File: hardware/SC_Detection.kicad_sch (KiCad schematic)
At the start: 46 parts, among them U11 REF2033, U12 LMV393LV, U13 INA181, U15 LMV393LV, U16 INA181, U17 LMV393LV, U18 INA181, U22 LMV393LV, U25 INA181

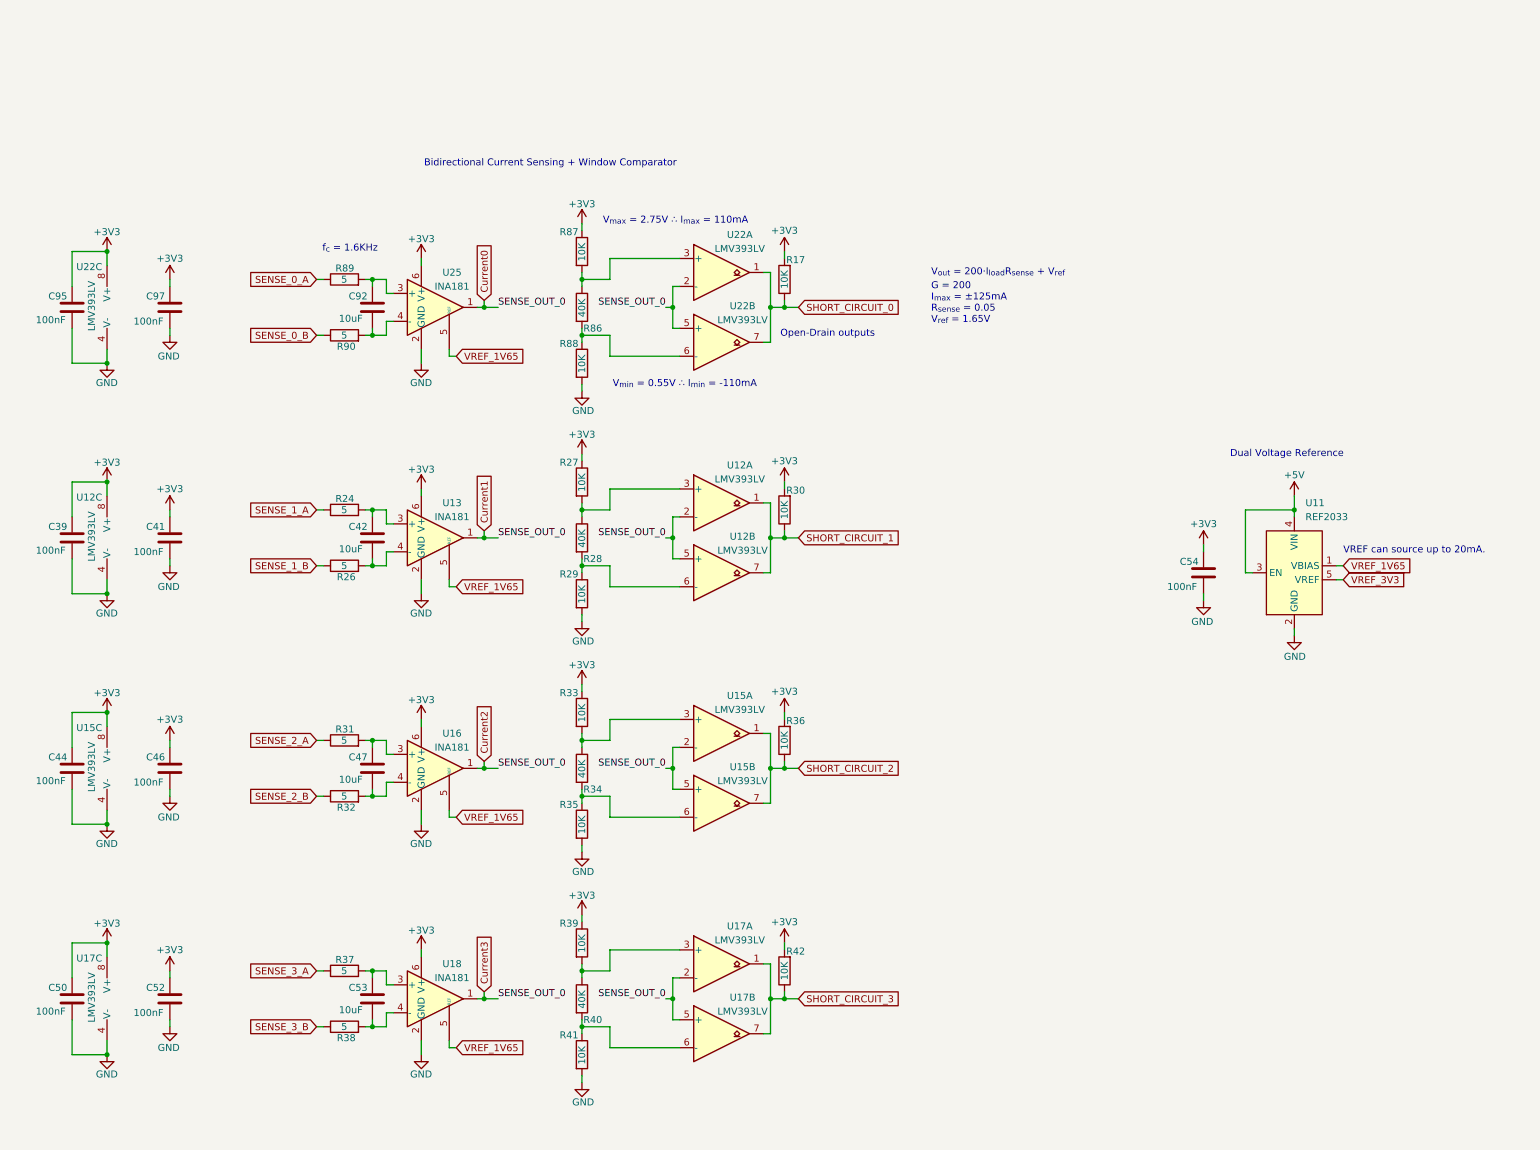
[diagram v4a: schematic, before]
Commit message: update short detection; draft bom
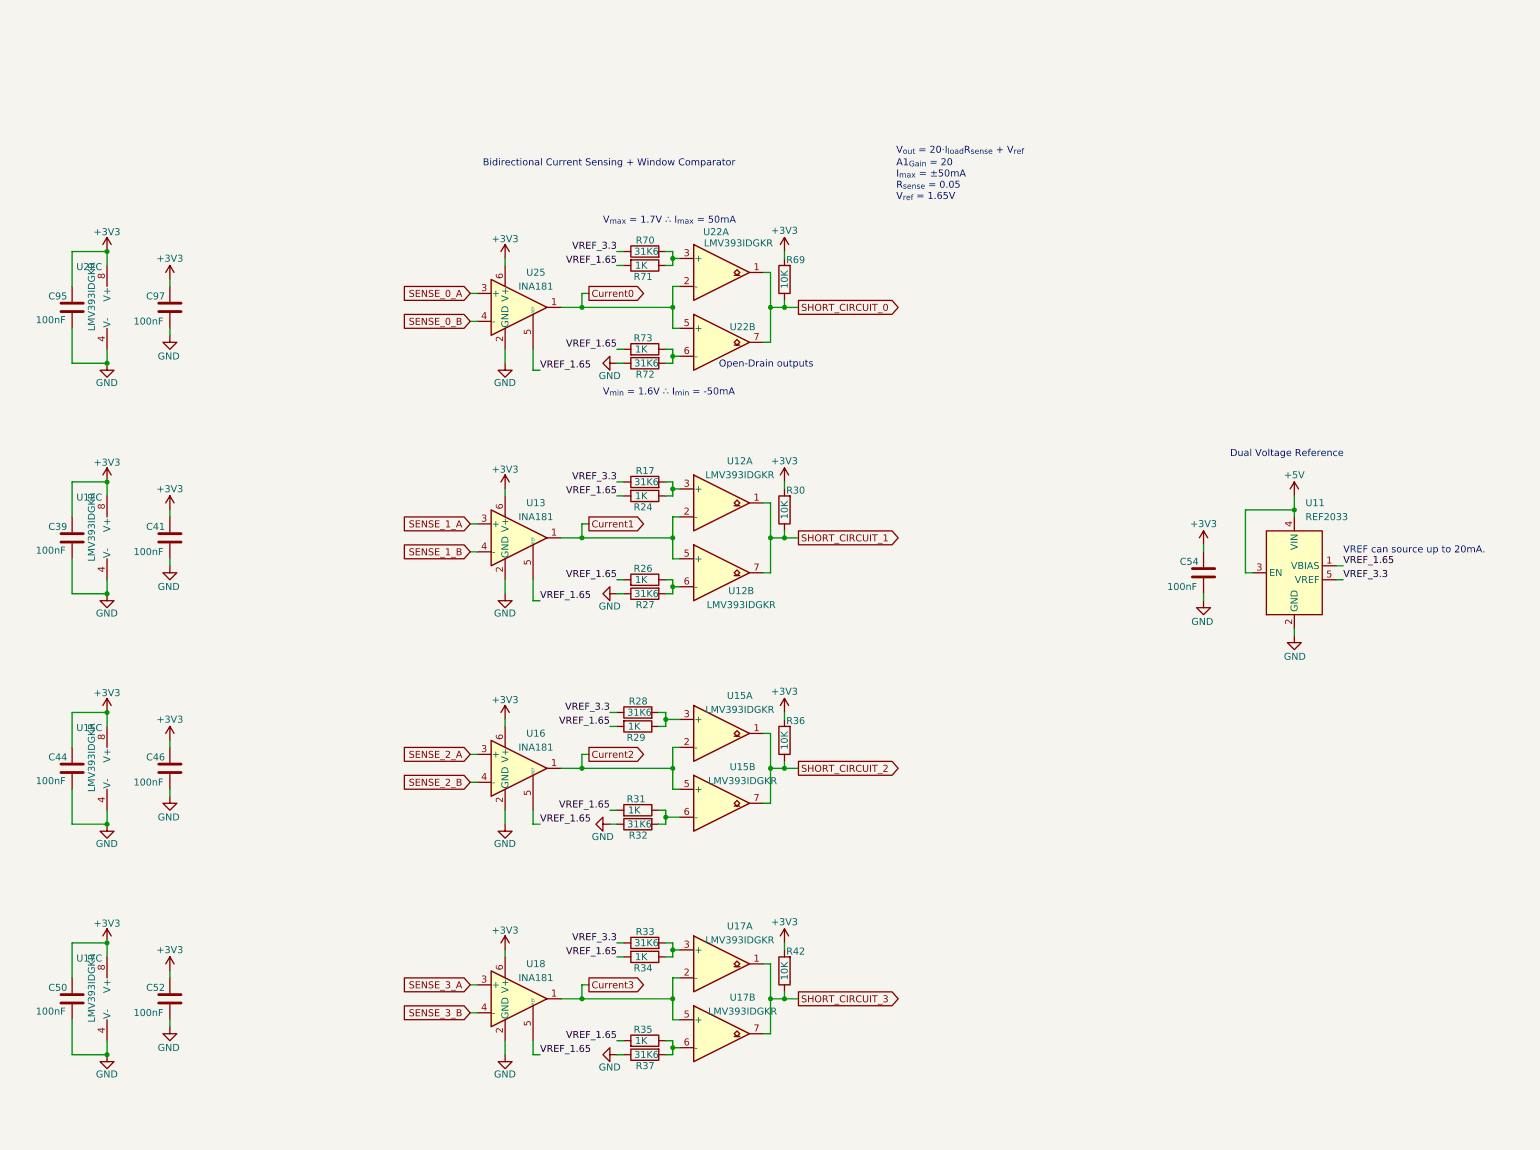
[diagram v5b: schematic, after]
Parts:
- removed C42, C47, C53, C92: 10uF, symbol Device:C
- removed R38, R89, R90: 5, symbol Device:R
- removed R39, R41, R87, R88: 10K, symbol Device:R
- removed R40, R86: 40K, symbol Device:R
- added R69: 10K, Resistor_SMD:R_0402_1005Metric, symbol Device:R
- added R70, R72: 31K6, Resistor_SMD:R_0402_1005Metric, symbol Device:R
- added R71, R73: 1K, Resistor_SMD:R_0402_1005Metric, symbol Device:R
- C39, C41, C44, C46, C50, C52, C54, C95, C97: footprint (none) -> Capacitor_SMD:C_0402_1005Metric; Link (none) -> https://www.digikey.com/en/products/detail/murata-electroni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; Manufacturer (none) -> Murata Electronics; Manufacturer Number (none) -> GRM155R71H104KE14D; Temperature Coefficient (none) -> X7R
- R17, R27, R33: value 10K -> 31K6; footprint (none) -> Resistor_SMD:R_0402_1005Metric
- R24, R26, R31: value 5 -> 1K; footprint (none) -> Resistor_SMD:R_0402_1005Metric
- R28: value 40K -> 31K6; footprint (none) -> Resistor_SMD:R_0402_1005Metric
- R29, R35: value 10K -> 1K; footprint (none) -> Resistor_SMD:R_0402_1005Metric
- R30, R36, R42: footprint (none) -> Resistor_SMD:R_0402_1005Metric
- R32, R37: value 5 -> 31K6; footprint (none) -> Resistor_SMD:R_0402_1005Metric
- R34: value 40K -> 1K; footprint (none) -> Resistor_SMD:R_0402_1005Metric
- U12, U15, U17, U22: value LMV393LV -> LMV393IDGKR; footprint (none) -> Package_SO:VSSOP-8_3x3mm_P0.65mm; Link (none) -> https://www.ti.com/general/docs/suppproductinfo.tsp?distId=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; Manufacturer Number LM393LVPWR -> LMV393IDGKR
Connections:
- net VREF_1V65 is gone; now on net VREF_1.65: U11.1 (VBIAS), U13.5 (REF), U16.5 (REF), U18.5 (REF), U25.5 (REF)
- net +3V3: now also R69.2; no longer R17.2, R27.1, R33.1
- net Current0: no longer U12.2 (-), U12.5 (+), U13.1, U15.2 (-), U15.5 (+), U16.1, U17.2 (-), U17.5 (+), U18.1
- net GND: now also R27.1, R32.1, R37.1, R72.1; no longer R29.2, R35.2
- net SENSE_0_A: now also U25.3 (+)
- net SENSE_0_B: now also U25.4 (-)
- net SENSE_1_A: now also U13.3 (+); no longer R24.1
- net SENSE_1_B: now also U13.4 (-); no longer R26.1
- net SENSE_2_A: now also U16.3 (+); no longer R31.1
- net SENSE_2_B: now also U16.4 (-); no longer R32.1
- net SENSE_3_A: now also U18.3 (+); no longer R37.1
- net SENSE_3_B: now also U18.4 (-)
- net SHORT_CIRCUIT_0: now also R69.1; no longer R17.1
- net at U22.3 (+): now also R70.2, R71.1
- net at U22.6 (-): now also R72.2, R73.1
- net at R28.2, R29.1: now also U15.3 (+); no longer U12.6 (-)
- net at R37.2: now also R35.1, U17.6 (-); no longer U18.3 (+)
- net at R33.2, R34.1: now also U17.3 (+); no longer U15.3 (+)
- net VREF_1.65: now reaches R24.2
- net VREF_1.65: now also R26.2, R29.2, R31.2, R34.2, R35.2, R71.2, R73.2; no longer U13.3 (+)
- net at R32.2: now also R31.1, U15.6 (-); no longer U16.4 (-)
- net VREF_3V3 renamed VREF_3.3
- net VREF_3.3: now also R17.1, R28.1, R33.1, R70.1
- new net: R26.1, R27.2, U12.6 (-)
- new net: R17.2, R24.1, U12.3 (+)
- new net Current1: U12.2 (-), U12.5 (+), U13.1
- new net Current2: U15.2 (-), U15.5 (+), U16.1
- new net Current3: U17.2 (-), U17.5 (+), U18.1
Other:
- note added: "A1_{Gain} = 20 I_{max} = ±50mA R_{sense} = 0.05 V_{ref} = 1.65V"
- note added: "V_{max} = 1.7V ∴ I_{max} = 50mA"
- note added: "V_{min} = 1.6V ∴ I_{min} = -50mA"
- note added: "V_{out} = 20·I_{load}R_{sense} + V_{ref}"
- note removed: "G = 200 I_{max} = ±125mA R_{sense} = 0.05 V_{ref} = 1.65V"
- note removed: "V_{max} = 2.75V ∴ I_{max} = 110mA"
- note removed: "V_{min} = 0.55V ∴ I_{min} = -110mA"
- note removed: "V_{out} = 200·I_{load}R_{sense} + V_{ref}"
- note removed: "f_{c} = 1.6KHz"
- moved on the sheet: U13, U16, U18, U25

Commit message: update board draft
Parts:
- renumbered C95 to C50, C39 to C51, C44 to C52, C50 to C53, C97 to C54, C41 to C55, C46 to C56, C52 to C57, C54 to C58, R28 to R39, R29 to R40, R31 to R41, R32 to R42, R70 to R43, R71 to R44, R73 to R45, R72 to R46, R17 to R47, R24 to R48, R26 to R49, R27 to R50, R33 to R51, R34 to R52, R35 to R53, R37 to R54, R69 to R55, R30 to R56, R36 to R57, R42 to R58, U22 to U13, U12 to U14, U17 to U16, U25 to U17, U13 to U18, U16 to U19, U18 to U20, U11 to U21
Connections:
- net +3V3 renamed +3.3V
- net +3.3V: no longer R58.2

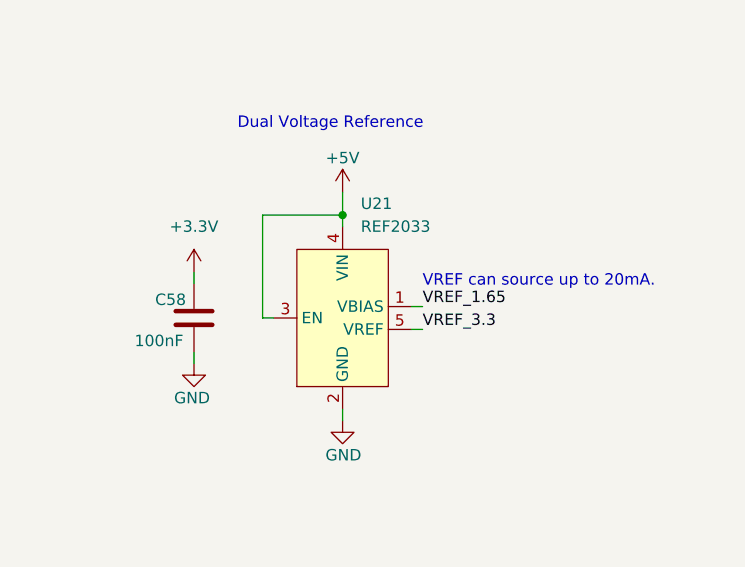
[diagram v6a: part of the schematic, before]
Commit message: draft power pours in internal layers
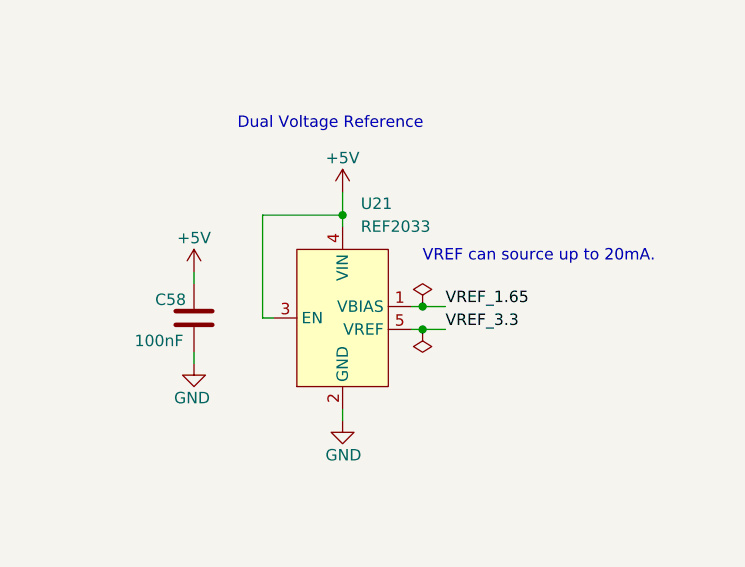
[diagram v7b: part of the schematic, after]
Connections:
- net +3.3V: no longer C58.1
- net +5V: now also C58.1
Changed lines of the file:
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@@
 	(text "VREF can source up to 20mA."
 		(exclude_from_sim no)
-		(at 252.73 91.948 0)
+		(at 252.73 89.154 0)
 		(effects
 			(font
@@
 	)
 	(junction
+		(at 252.73 93.98)
+		(diameter 0)
+		(color 0 0 0 0)
+	)
+	(junction
 		(at 114.3 88.9)
 		(diameter 0)
@@
 	)
 	(junction
+		(at 252.73 96.52)
+		(diameter 0)
+		(color 0 0 0 0)
+	)
+	(junction
 		(at 114.3 172.72)
 		(diameter 0)
@@
 	(wire
 		(pts
+			(xy 252.73 93.98) (xy 255.27 93.98)
+		)
+		(stroke
+			(width 0)
+			(type default)
+		)
+	)
+	(wire
+		(pts
 			(xy 251.46 93.98) (xy 252.73 93.98)
 		)
@@
 	(wire
 		(pts
+			(xy 252.73 96.52) (xy 255.27 96.52)
+		)
+		(stroke
+			(width 0)
+			(type default)
+		)
+	)
+	(wire
+		(pts
 			(xy 21.59 134.62) (xy 21.59 140.97)
 		)
@@
 	)
 	(label "VREF_3.3"
-		(at 252.73 96.52 0)
+		(at 255.27 96.52 0)
 		(effects
 			(font
@@
 	)
 	(label "VREF_1.65"
-		(at 252.73 93.98 0)
+		(at 255.27 93.98 0)
 		(effects
 			(font
@@
 	)
 	(symbol
+		(lib_id "power:PWR_FLAG")
+		(at 252.73 96.52 180)
+		(unit 1)
+		(exclude_from_sim no)
+		(in_bom yes)
+		(on_board yes)
+		(dnp no)
+		(fields_autoplaced yes)
+		(property "Reference" "#FLG08"
+			(at 252.73 98.425 0)
+			(effects
+				(font
+					(size 1.27 1.27)
+				)
+				(hide yes)
+			)
+		)
+		(property "Value" "PWR_FLAG"
+			(at 252.73 101.6 0)
+			(effects
+				(font
+					(size 1.27 1.27)
+				)
+				(hide yes)
+			)
+		)
+		(property "Footprint" ""
+			(at 252.73 96.52 0)
+			(effects
+				(font
+					(size 1.27 1.27)
+				)
+				(hide yes)
+			)
+		)
+		(property "Datasheet" "~"
+			(at 252.73 96.52 0)
+			(effects
+				(font
+					(size 1.27 1.27)
+				)
+				(hide yes)
+			)
+		)
+		(property "Description" "Special symbol for telling ERC where power comes from"
+			(at 252.73 96.52 0)
+			(effects
+				(font
+					(size 1.27 1.27)
+				)
+				(hide yes)
+			)
+		)
+		(pin "1"
+		)
+		(instances
+			(project ""
+				(path "/6b47c519-21c4-43bd-9777-b273999e4447/1945aa77-a929-44fd-b3b6-12787633d2f2"
+					(reference "#FLG08")
+					(unit 1)
+				)
+			)
+		)
+	)
+	(symbol
 		(lib_id "power:+3.3V")
 		(at 151.13 161.29 0)
@@
 	)
 	(symbol
-		(lib_id "power:+3.3V")
-		(at 227.33 90.17 0)
-		(unit 1)
-		(exclude_from_sim no)
-		(in_bom yes)
-		(on_board yes)
-		(dnp no)
-		(fields_autoplaced yes)
-		(property "Reference" "#PWR01"
-			(at 227.33 93.98 0)
-			(effects
-				(font
-					(size 1.27 1.27)
-				)
-				(hide yes)
-			)
-		)
-		(property "Value" "+3.3V"
-			(at 227.33 85.09 0)
-			(effects
-				(font
-					(size 1.27 1.27)
-				)
-			)
-		)
-		(property "Footprint" ""
-			(at 227.33 90.17 0)
-			(effects
-				(font
-					(size 1.27 1.27)
-				)
-				(hide yes)
-			)
-		)
-		(property "Datasheet" ""
-			(at 227.33 90.17 0)
-			(effects
-				(font
-					(size 1.27 1.27)
-				)
-				(hide yes)
-			)
-		)
-		(property "Description" "Power symbol creates a global label with name \"+3.3V\""
-			(at 227.33 90.17 0)
-			(effects
-				(font
-					(size 1.27 1.27)
-				)
-				(hide yes)
-			)
-		)
-		(pin "1"
-		)
-		(instances
-			(project ""
-				(path "/6b47c519-21c4-43bd-9777-b273999e4447/1945aa77-a929-44fd-b3b6-12787633d2f2"
-					(reference "#PWR01")
-					(unit 1)
-				)
-			)
-		)
-	)
-	(symbol
 		(lib_id "Comparator:LMV393")
 		(at 139.7 179.07 0)
@@
 	)
 	(symbol
+		(lib_id "power:+5V")
+		(at 227.33 90.17 0)
+		(unit 1)
+		(exclude_from_sim no)
+		(in_bom yes)
+		(on_board yes)
+		(dnp no)
+		(property "Reference" "#PWR01"
+			(at 227.33 93.98 0)
+			(effects
+				(font
+					(size 1.27 1.27)
+				)
+				(hide yes)
+			)
+		)
+		(property "Value" "+5V"
+			(at 227.33 86.36 0)
+			(effects
+				(font
+					(size 1.27 1.27)
+				)
+			)
+		)
+		(property "Footprint" ""
+			(at 227.33 90.17 0)
+			(effects
+				(font
+					(size 1.27 1.27)
+				)
+				(hide yes)
+			)
+		)
+		(property "Datasheet" ""
+			(at 227.33 90.17 0)
+			(effects
+				(font
+					(size 1.27 1.27)
+				)
+				(hide yes)
+			)
+		)
+		(property "Description" "Power symbol creates a global label with name \"+5V\""
+			(at 227.33 90.17 0)
+			(effects
+				(font
+					(size 1.27 1.27)
+				)
+				(hide yes)
+			)
+		)
+		(pin "1"
+		)
+		(instances
+			(project "harp.device.quad.dac"
+				(path "/6b47c519-21c4-43bd-9777-b273999e4447/1945aa77-a929-44fd-b3b6-12787633d2f2"
+					(reference "#PWR01")
+					(unit 1)
+				)
+			)
+		)
+	)
+	(symbol
 		(lib_id "power:+3.3V")
 		(at 151.13 78.74 0)
@@
 				)
 			)
+		)
+	)
+	(symbol
+		(lib_id "power:PWR_FLAG")
+		(at 252.73 93.98 0)
+		(unit 1)
+		(exclude_from_sim no)
+		(in_bom yes)
+		(on_board yes)
+		(dnp no)
+		(fields_autoplaced yes)
+		(property "Reference" "#FLG07"
+			(at 252.73 92.075 0)
+			(effects
+				(font
+					(size 1.27 1.27)
+				)
+				(hide yes)
+			)
+		)
+		(property "Value" "PWR_FLAG"
+			(at 252.73 88.9 0)
+			(effects
+				(font
+					(size 1.27 1.27)
+				)
+				(hide yes)
+			)
+		)
+		(property "Footprint" ""
+			(at 252.73 93.98 0)
+			(effects
+				(font
+					(size 1.27 1.27)
+				)
+				(hide yes)
+			)
+		)
+		(property "Datasheet" "~"
+			(at 252.73 93.98 0)
+			(effects
+				(font
+					(size 1.27 1.27)
+				)
+				(hide yes)
+			)
+		)
+		(property "Description" "Special symbol for telling ERC where power comes from"
+			(at 252.73 93.98 0)
+			(effects
+				(font
+					(size 1.27 1.27)
+				)
+				(hide yes)
+			)
+		)
+		(pin "1"
+		)
+		(instances
+			(project ""
+				(path "/6b47c519-21c4-43bd-9777-b273999e4447/1945aa77-a929-44fd-b3b6-12787633d2f2"
+					(reference "#FLG07")
+					(unit 1)
+				)
+			)

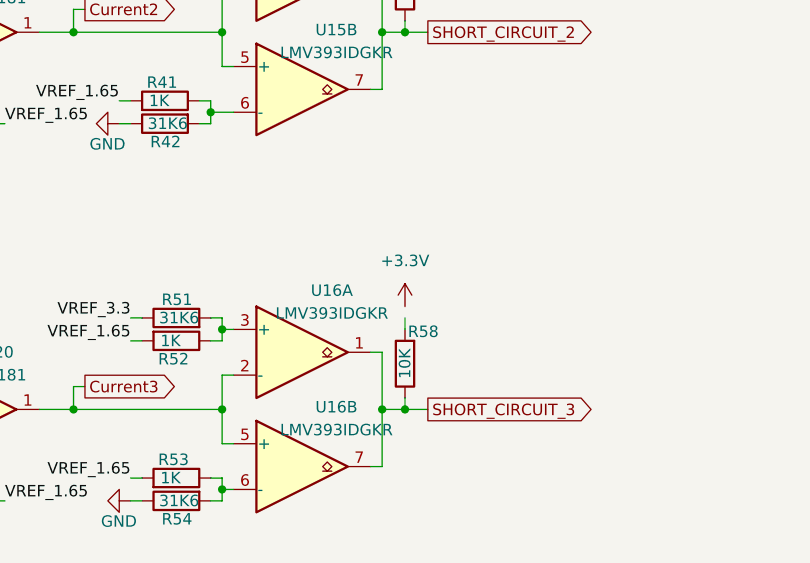
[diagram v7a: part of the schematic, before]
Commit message: fix sd card order; finish pcb draft
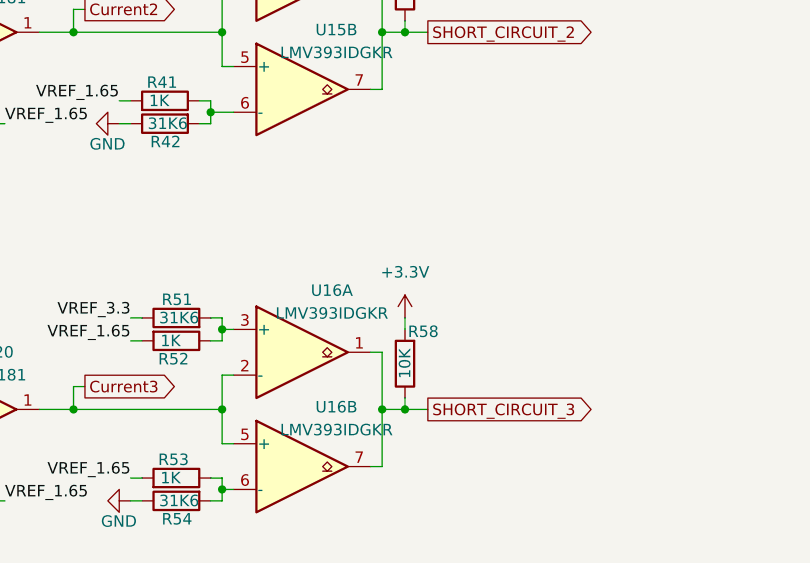
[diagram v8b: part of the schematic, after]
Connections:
- net +3.3V: now also R58.2
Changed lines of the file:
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@@
 	(symbol
 		(lib_id "power:+3.3V")
-		(at 151.13 161.29 0)
+		(at 151.13 162.56 0)
 		(unit 1)
 		(exclude_from_sim no)
@@
 		(fields_autoplaced yes)
 		(property "Reference" "#PWR0131"
-			(at 151.13 165.1 0)
+			(at 151.13 166.37 0)
 			(effects
 				(font
@@
 		)
 		(property "Value" "+3.3V"
-			(at 151.13 156.21 0)
+			(at 151.13 157.48 0)
 			(effects
 				(font
@@
 		)
 		(property "Footprint" ""
-			(at 151.13 161.29 0)
+			(at 151.13 162.56 0)
 			(effects
 				(font
@@
 		)
 		(property "Datasheet" ""
-			(at 151.13 161.29 0)
+			(at 151.13 162.56 0)
 			(effects
 				(font
@@
 		)
 		(property "Description" "Power symbol creates a global label with name \"+3.3V\""
-			(at 151.13 161.29 0)
+			(at 151.13 162.56 0)
 			(effects
 				(font
